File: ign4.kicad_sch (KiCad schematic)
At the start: 15 parts, among them U41 MIC4427, U42 MIC4427

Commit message: update
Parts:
- removed C9: 1u, symbol Device:C
- added R26, R32, R34, R35: 2k7, Resistor_SMD:R_0805_2012Metric, symbol Device:R
- added U31 (x4): RED, LED_SMD:LED_0805_2012Metric, symbol Device:LED
- C5: footprint (none) -> Capacitor_SMD:C_1206_3216Metric
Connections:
- net GND: now also U31.1 (K), U31.1 (K), U31.1 (K), U31.1 (K)
- net at R123.2, U41.5 (OUT_B): now also R32.1
- net at R122.2, U41.7 (OUT_A): now also R26.1
- net at R125.2, U42.5 (OUT_B): now also R35.1
- net at R124.2, U42.7 (OUT_A): now also R34.1
- net +5V renamed V_SUP
- new net: R35.2, U31.2 (A)
- new net: R26.2, U31.2 (A)
- new net: R32.2, U31.2 (A)
- new net: R34.2, U31.2 (A)
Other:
- moved on the sheet: C5, C96, C97, C98, C99, R122, R123, R124, R125

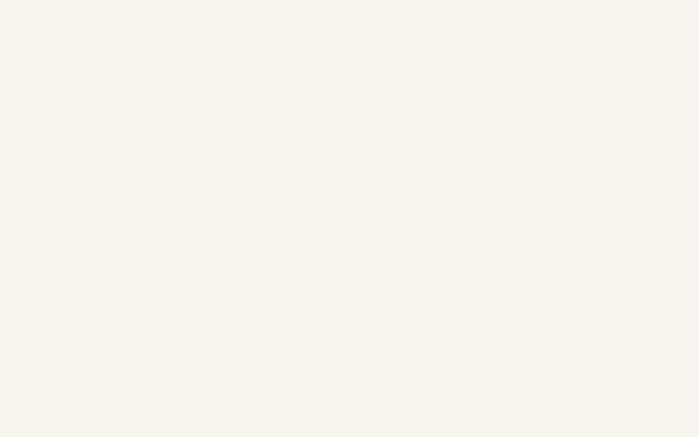
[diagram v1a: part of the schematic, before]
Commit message: Updates - Route digital inputs to connector - Add optional VR conditioner - Second Enable for H-Bridge
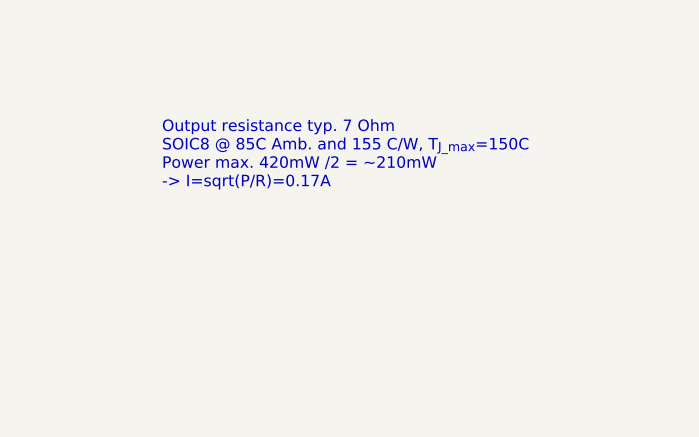
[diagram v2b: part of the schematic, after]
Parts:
- R122, R123, R124, R125: footprint Resistor_SMD:R_0805_2012Metric -> Resistor_SMD:R_2512_6332Metric
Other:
- note added: "Output resistance typ. 7 Ohm SOIC8 @ 85C Amb. and 155 C/W, T_{J_max}=150C Power max. 420mW /2 = ~210mW -> I=sqrt(P/R)=0.17A"
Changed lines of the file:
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@@
     (stroke (width 0) (type default))
+  )
+  (text "Output resistance typ. 7 Ohm\nSOIC8 @ 85C Amb. and 155 C/W, T_{J_max}=150C\nPower max. 420mW /2 = ~210mW\n-> I=sqrt(P/R)=0.17A"
+    (at 163.195 40.005 0)
+    (effects (font (size 1.27 1.27)) (justify left bottom))
   )
   (label "V_SUP" (at 76.835 32.385 90) (fields_autoplaced)
@@
       (effects (font (size 1.27 1.27)))
     )
-    (property "Footprint" "Resistor_SMD:R_0805_2012Metric" (at 123.19 42.672 90)
+    (property "Footprint" "Resistor_SMD:R_2512_6332Metric" (at 123.19 42.672 90)
       (effects (font (size 1.27 1.27)) hide)
     )
@@
       (effects (font (size 1.27 1.27)))
     )
-    (property "Footprint" "Resistor_SMD:R_0805_2012Metric" (at 123.19 47.752 90)
+    (property "Footprint" "Resistor_SMD:R_2512_6332Metric" (at 123.19 47.752 90)
       (effects (font (size 1.27 1.27)) hide)
     )
@@
       (effects (font (size 1.27 1.27)))
     )
-    (property "Footprint" "Resistor_SMD:R_0805_2012Metric" (at 123.19 80.772 90)
+    (property "Footprint" "Resistor_SMD:R_2512_6332Metric" (at 123.19 80.772 90)
       (effects (font (size 1.27 1.27)) hide)
     )
@@
       (effects (font (size 1.27 1.27)))
     )
-    (property "Footprint" "Resistor_SMD:R_0805_2012Metric" (at 123.19 85.852 90)
-      (effects (font (size 1.27 1.27)) hide)
-    )
+    (property "Footprint" "Resistor_SMD:R_2512_6332Metric" (at 123.19 85.852 90)
+      (effects (font (size 1.27 1.27)) hide)
+    )

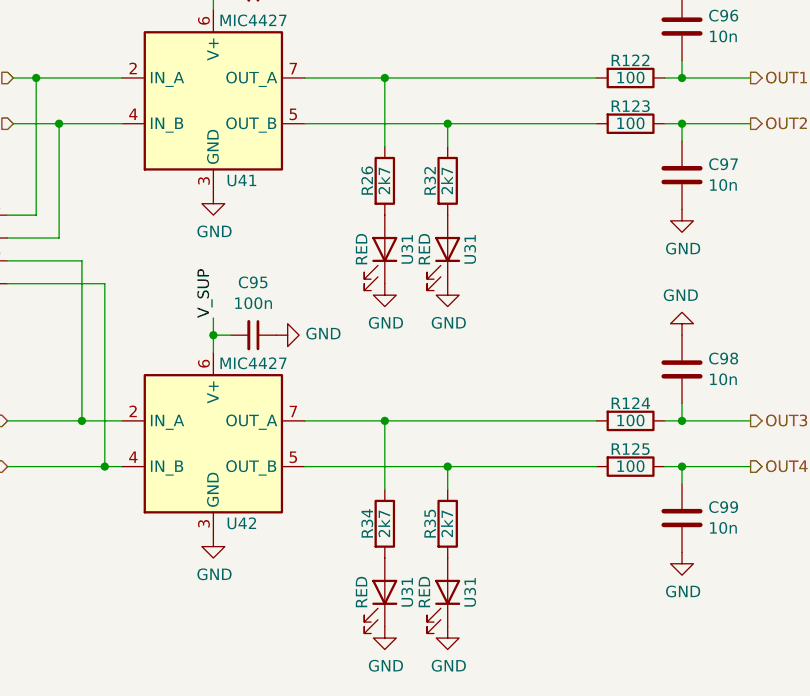
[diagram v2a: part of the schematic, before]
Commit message: USB jack, parts and LCSC numbers, headphone jack
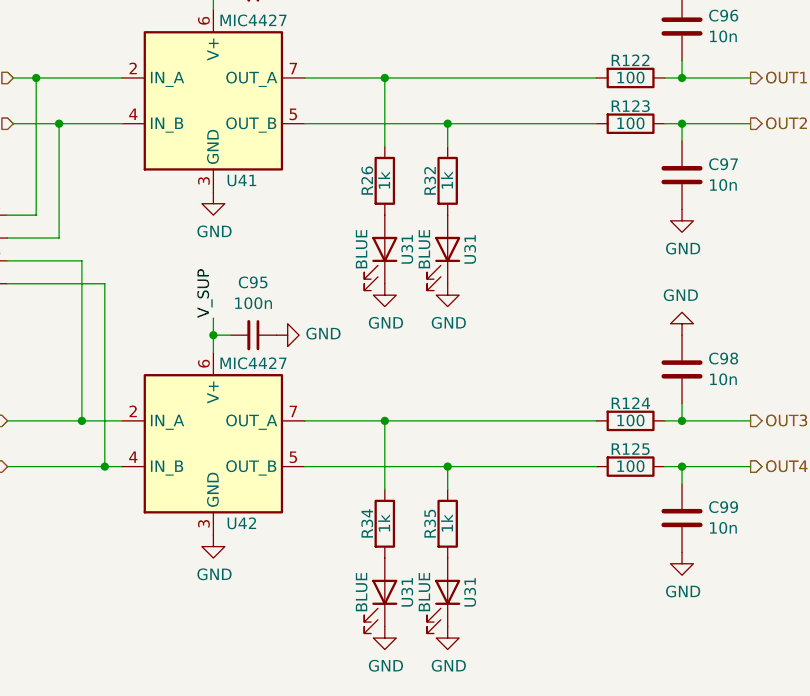
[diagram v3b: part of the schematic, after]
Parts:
- C5: footprint Capacitor_SMD:C_1206_3216Metric -> Capacitor_SMD:C_0603_1608Metric; LCSC (none) -> C15849
- R122, R123, R124, R125: LCSC C17408 -> C2907569
- R26, R32, R34, R35: value 2k7 -> 1k; footprint Resistor_SMD:R_0805_2012Metric -> Resistor_SMD:R_0402_1005Metric; LCSC C17408 -> C106235
- U31: value RED -> BLUE; footprint LED_SMD:LED_0805_2012Metric -> LED_SMD:LED_0603_1608Metric; LCSC (none) -> C72041
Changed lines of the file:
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@@
       (effects (font (size 1.27 1.27)) hide)
     )
-    (property "LCSC" "C17408" (at 123.19 44.45 0)
+    (property "LCSC" "C2907569" (at 123.19 44.45 0)
       (effects (font (size 1.27 1.27)) hide)
     )
@@
       (effects (font (size 1.27 1.27)) hide)
     )
-    (property "LCSC" "C17408" (at 123.19 49.53 0)
+    (property "LCSC" "C2907569" (at 123.19 49.53 0)
       (effects (font (size 1.27 1.27)) hide)
     )
@@
       (effects (font (size 1.27 1.27)) hide)
     )
-    (property "LCSC" "C17408" (at 123.19 82.55 0)
+    (property "LCSC" "C2907569" (at 123.19 82.55 0)
       (effects (font (size 1.27 1.27)) hide)
     )
@@
       (effects (font (size 1.27 1.27)) hide)
     )
-    (property "LCSC" "C17408" (at 123.19 87.63 0)
+    (property "LCSC" "C2907569" (at 123.19 87.63 0)
       (effects (font (size 1.27 1.27)) hide)
     )
@@
       (effects (font (size 1.27 1.27)))
     )
-    (property "Value" "2k7" (at 102.87 93.98 90)
-      (effects (font (size 1.27 1.27)))
-    )
-    (property "Footprint" "Resistor_SMD:R_0805_2012Metric" (at 101.092 93.98 90)
+    (property "Value" "1k" (at 102.87 93.98 90)
+      (effects (font (size 1.27 1.27)))
+    )
+    (property "Footprint" "Resistor_SMD:R_0402_1005Metric" (at 101.092 93.98 90)
       (effects (font (size 1.27 1.27)) hide)
     )
@@
       (effects (font (size 1.27 1.27)) hide)
     )
-    (property "LCSC" "C17408" (at 102.87 93.98 0)
+    (property "LCSC" "C106235" (at 102.87 93.98 0)
       (effects (font (size 1.27 1.27)) hide)
     )
@@
       (effects (font (size 1.27 1.27)) (justify right))
     )
-    (property "Footprint" "Capacitor_SMD:C_1206_3216Metric" (at 56.1848 22.225 0)
+    (property "Footprint" "Capacitor_SMD:C_0603_1608Metric" (at 56.1848 22.225 0)
       (effects (font (size 1.27 1.27)) hide)
     )
@@
       (effects (font (size 1.27 1.27)) hide)
     )
+    (property "LCSC" "C15849" (at 57.15 26.035 0)
+      (effects (font (size 1.27 1.27)) hide)
+    )
     (pin "1")
     (pin "2")
@@
       (effects (font (size 1.27 1.27)))
     )
-    (property "Value" "2k7" (at 95.885 55.88 90)
-      (effects (font (size 1.27 1.27)))
-    )
-    (property "Footprint" "Resistor_SMD:R_0805_2012Metric" (at 94.107 55.88 90)
+    (property "Value" "1k" (at 95.885 55.88 90)
+      (effects (font (size 1.27 1.27)))
+    )
+    (property "Footprint" "Resistor_SMD:R_0402_1005Metric" (at 94.107 55.88 90)
       (effects (font (size 1.27 1.27)) hide)
     )
@@
       (effects (font (size 1.27 1.27)) hide)
     )
-    (property "LCSC" "C17408" (at 95.885 55.88 0)
+    (property "LCSC" "C106235" (at 95.885 55.88 0)
       (effects (font (size 1.27 1.27)) hide)
     )
@@
       (effects (font (size 1.27 1.27)))
     )
-    (property "Value" "RED" (at 100.33 101.6 0)
-      (effects (font (size 1.27 1.27)))
-    )
-    (property "Footprint" "LED_SMD:LED_0805_2012Metric" (at 102.87 101.6 0)
+    (property "Value" "BLUE" (at 100.33 101.6 0)
+      (effects (font (size 1.27 1.27)))
+    )
+    (property "Footprint" "LED_SMD:LED_0603_1608Metric" (at 102.87 101.6 0)
       (effects (font (size 1.27 1.27)) hide)
     )
     (property "Datasheet" "" (at 102.87 101.6 0)
       (effects (font (size 1.27 1.27)))
+    )
+    (property "LCSC" "C72041" (at 102.87 101.6 0)
+      (effects (font (size 1.27 1.27)) hide)
     )
     (pin "1")
@@
       (effects (font (size 1.27 1.27)))
     )
-    (property "Value" "2k7" (at 102.87 55.88 90)
-      (effects (font (size 1.27 1.27)))
-    )
-    (property "Footprint" "Resistor_SMD:R_0805_2012Metric" (at 101.092 55.88 90)
+    (property "Value" "1k" (at 102.87 55.88 90)
+      (effects (font (size 1.27 1.27)))
+    )
+    (property "Footprint" "Resistor_SMD:R_0402_1005Metric" (at 101.092 55.88 90)
       (effects (font (size 1.27 1.27)) hide)
     )
@@
       (effects (font (size 1.27 1.27)) hide)
     )
-    (property "LCSC" "C17408" (at 102.87 55.88 0)
+    (property "LCSC" "C106235" (at 102.87 55.88 0)
       (effects (font (size 1.27 1.27)) hide)
     )
@@
       (effects (font (size 1.27 1.27)))
     )
-    (property "Value" "RED" (at 93.345 63.5 0)
-      (effects (font (size 1.27 1.27)))
-    )
-    (property "Footprint" "LED_SMD:LED_0805_2012Metric" (at 95.885 63.5 0)
+    (property "Value" "BLUE" (at 93.345 63.5 0)
+      (effects (font (size 1.27 1.27)))
+    )
+    (property "Footprint" "LED_SMD:LED_0603_1608Metric" (at 95.885 63.5 0)
       (effects (font (size 1.27 1.27)) hide)
     )
     (property "Datasheet" "" (at 95.885 63.5 0)
       (effects (font (size 1.27 1.27)))
+    )
+    (property "LCSC" "C72041" (at 95.885 63.5 0)
+      (effects (font (size 1.27 1.27)) hide)
     )
     (pin "1")
@@
       (effects (font (size 1.27 1.27)))
     )
-    (property "Value" "RED" (at 100.33 63.5 0)
-      (effects (font (size 1.27 1.27)))
-    )
-    (property "Footprint" "LED_SMD:LED_0805_2012Metric" (at 102.87 63.5 0)
+    (property "Value" "BLUE" (at 100.33 63.5 0)
+      (effects (font (size 1.27 1.27)))
+    )
+    (property "Footprint" "LED_SMD:LED_0603_1608Metric" (at 102.87 63.5 0)
       (effects (font (size 1.27 1.27)) hide)
     )
     (property "Datasheet" "" (at 102.87 63.5 0)
       (effects (font (size 1.27 1.27)))
+    )
+    (property "LCSC" "C72041" (at 102.87 63.5 0)
+      (effects (font (size 1.27 1.27)) hide)
     )
     (pin "1")
@@
       (effects (font (size 1.27 1.27)))
     )
-    (property "Value" "2k7" (at 95.885 93.98 90)
-      (effects (font (size 1.27 1.27)))
-    )
-    (property "Footprint" "Resistor_SMD:R_0805_2012Metric" (at 94.107 93.98 90)
+    (property "Value" "1k" (at 95.885 93.98 90)
+      (effects (font (size 1.27 1.27)))
+    )
+    (property "Footprint" "Resistor_SMD:R_0402_1005Metric" (at 94.107 93.98 90)
       (effects (font (size 1.27 1.27)) hide)
     )
@@
       (effects (font (size 1.27 1.27)) hide)
     )
-    (property "LCSC" "C17408" (at 95.885 93.98 0)
+    (property "LCSC" "C106235" (at 95.885 93.98 0)
       (effects (font (size 1.27 1.27)) hide)
     )
@@
       (effects (font (size 1.27 1.27)))
     )
-    (property "Value" "RED" (at 93.345 101.6 0)
-      (effects (font (size 1.27 1.27)))
-    )
-    (property "Footprint" "LED_SMD:LED_0805_2012Metric" (at 95.885 101.6 0)
+    (property "Value" "BLUE" (at 93.345 101.6 0)
+      (effects (font (size 1.27 1.27)))
+    )
+    (property "Footprint" "LED_SMD:LED_0603_1608Metric" (at 95.885 101.6 0)
       (effects (font (size 1.27 1.27)) hide)
     )
@@
       (effects (font (size 1.27 1.27)))
     )
-    (pin "1")
+    (property "LCSC" "C72041" (at 95.885 101.6 0)
+      (effects (font (size 1.27 1.27)) hide)
+    )
+    (pin "1")

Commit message: Add Stepper, fix Connector, add Testpoints, several changes
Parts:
- R26, R32, R34, R35: LCSC C106235 -> C11702
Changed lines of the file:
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@@
       (effects (font (size 1.27 1.27)) hide)
     )
-    (property "LCSC" "C106235" (at 102.87 93.98 0)
+    (property "LCSC" "C11702" (at 102.87 93.98 0)
       (effects (font (size 1.27 1.27)) hide)
     )
@@
       (effects (font (size 1.27 1.27)) hide)
     )
-    (property "LCSC" "C106235" (at 95.885 55.88 0)
+    (property "LCSC" "C11702" (at 95.885 55.88 0)
       (effects (font (size 1.27 1.27)) hide)
     )
@@
       (effects (font (size 1.27 1.27)) hide)
     )
-    (property "LCSC" "C106235" (at 102.87 55.88 0)
+    (property "LCSC" "C11702" (at 102.87 55.88 0)
       (effects (font (size 1.27 1.27)) hide)
     )
@@
       (effects (font (size 1.27 1.27)) hide)
     )
-    (property "LCSC" "C106235" (at 95.885 93.98 0)
-      (effects (font (size 1.27 1.27)) hide)
-    )
+    (property "LCSC" "C11702" (at 95.885 93.98 0)
+      (effects (font (size 1.27 1.27)) hide)
+    )
